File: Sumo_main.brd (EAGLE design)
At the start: 70 x 45 mm, 59 parts, among them IC1 TL331, T1 0603-PHOTO-TRANS, T2 0603-PHOTO-TRANS, U1 ATMEGA8U2AU, U2 SN65HVD3082, U3 LM339D, X2 RS485, Y1 16MHz

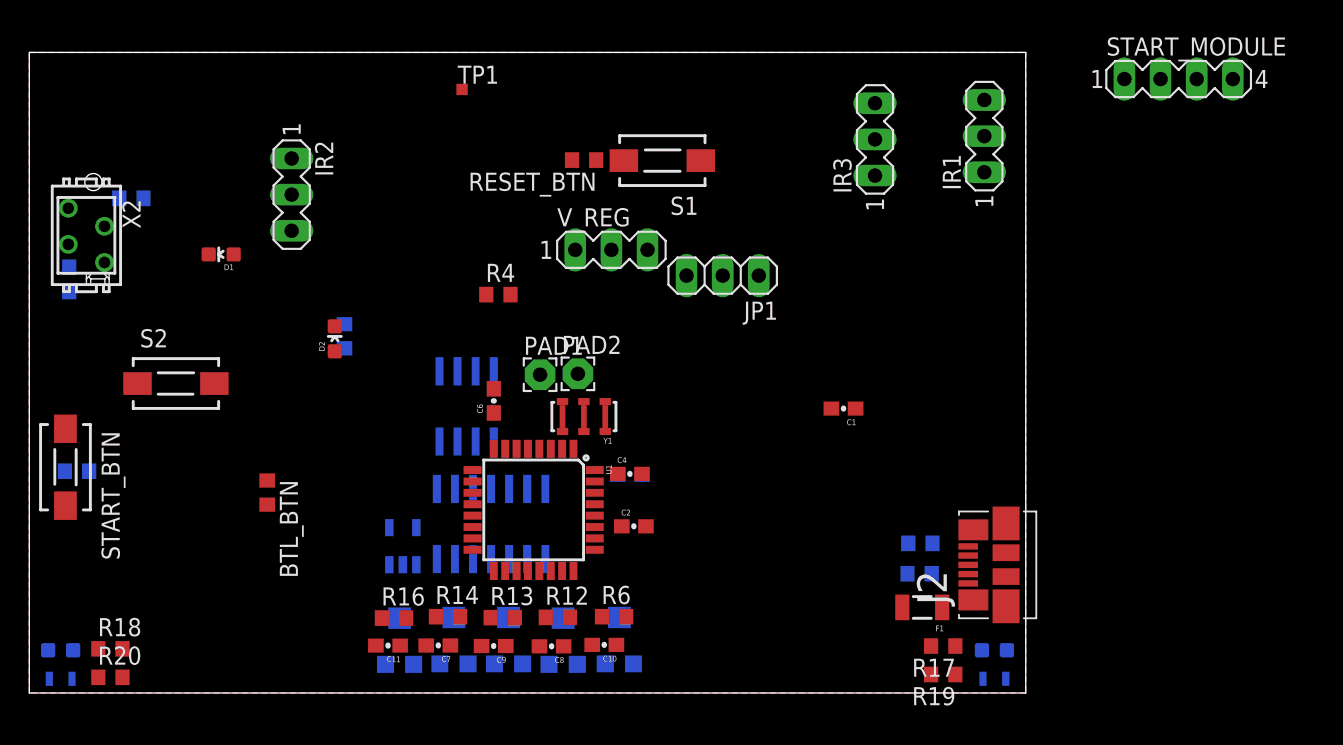
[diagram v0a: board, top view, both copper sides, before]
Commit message: Board redesign. TODO: Connect HWB
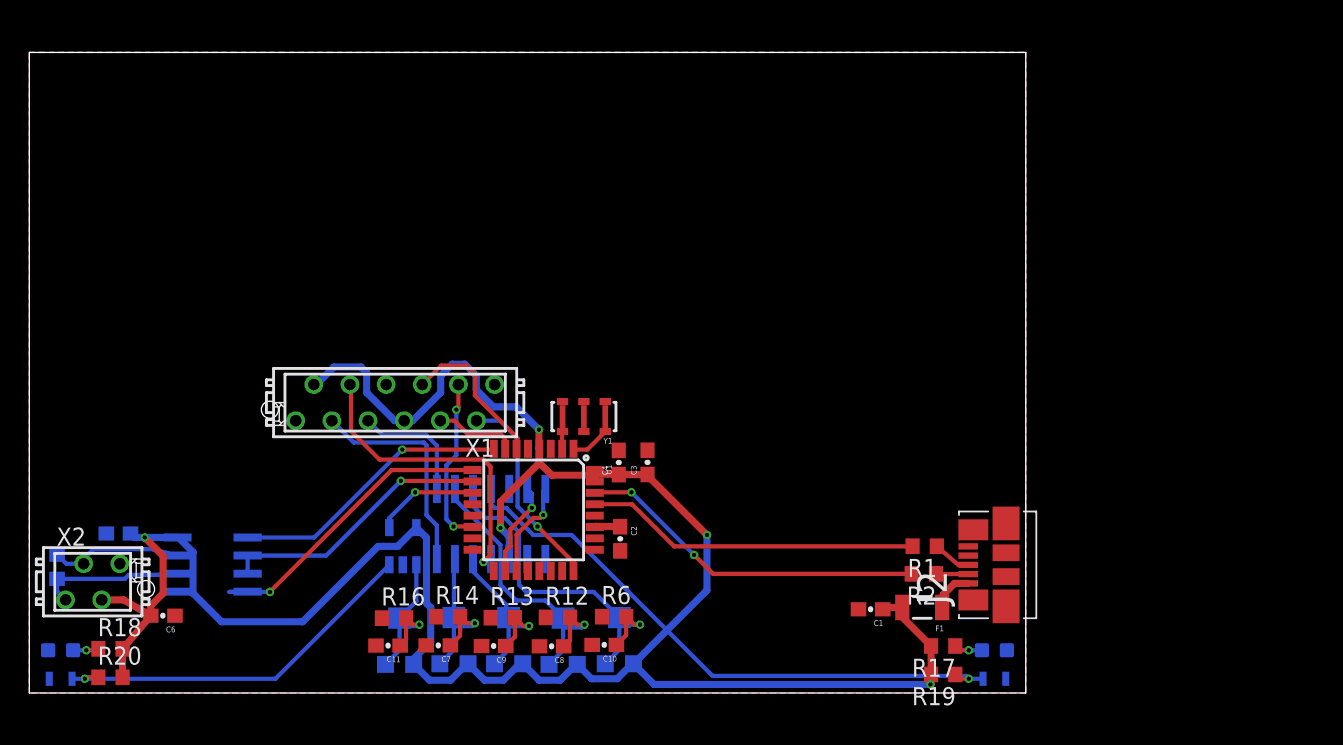
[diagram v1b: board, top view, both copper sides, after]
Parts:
- removed BTL_BTN, R7, RESET_BTN: 10K, resistor:R0603
- removed D1, D2: (no value), SparkFun-LED:LED-0603
- removed IR1, IR2, IR3, V_REG: (no value), con-lstb:MA03-1
- removed JP1: (no value), pinhead:1X03
- removed PAD1, PAD2: (no value), wirepad:2,15/1,0
- removed R4, R5: 1K, resistor:R0603
- removed S1, S2, START_BTN: DTSM-3, switch-tact:DTSM-3
- removed START_MODULE: (no value), con-lstb:MA04-1
- removed TP1: TPSQTP08SQ, testpad:TP08SQ
- added X1: MICROMATCH-12, con-amp-micromatch:MICROMATCH-12
- moved C6 27.7 mm to (9.38, 5.43), turned to 180 degrees
- moved R8 26.4 mm to (1.95, 8.87), turned to 270 degrees
- moved X2 24.3 mm to (4.45, 7.81), turned to 0 degrees
- moved U2 21.0 mm to (12.9, 9.02), turned to 0 degrees
- moved C5 18.2 mm to (6.26, 11.2), turned to 180 degrees
- moved C1 14.2 mm to (59.1, 5.88)
- moved C3 1.51 mm to (43.4, 16.2), flipped to the top, turned to 90 degrees
- moved C2 1.30 mm to (41.5, 10.8), turned to 270 degrees
- moved C4 1.12 mm to (41.4, 16.2), turned to 90 degrees
- moved R1 0.36 mm to (62.9, 10.3), flipped to the top, turned to 180 degrees
- moved R2 0.30 mm to (62.8, 8.37), flipped to the top, turned to 180 degrees
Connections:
- removed net LED1: R4.2, U1.5
- removed net LED2: R5.2, U1.26
- removed net N$10: D1.A, R4.1
- removed net N$12: F1.2, JP1.1
- removed net N$13: BTL_BTN.2, S2.2, U1.13
- removed net N$14: JP1.3, V_REG.3
- removed net N$17: U1.25
- removed net N$23: PAD1.1, V_REG.1
- removed net N$4: RESET_BTN.1, S1.2, U1.24
- removed net N$8: R7.1, START_BTN.2, U1.14
- removed net N$9: D2.A, R5.1
- new net HWB: U1.13, X1.12
- new net RESET: U1.24, X1.11
- new net START_BTN: U1.14, X1.10
- net GND: now also X1.1, X1.6; no longer D1.C, D2.C, IR1.2, IR2.2, IR3.2, PAD2.1, S1.1, S2.1, START_BTN.1, START_MODULE.2, V_REG.2
- net KILL: now also U1.6, X1.8; no longer START_MODULE.4, U1.23
- net START: now also U1.7, X1.9; no longer START_MODULE.3, U1.22
- net V01: now also X1.3; no longer IR1.3
- net V02: now also X1.4; no longer IR2.3
- net V03: now also X1.5; no longer IR3.3
- net VCC: now also F1.2, X1.2, X1.7; no longer BTL_BTN.1, IR1.1, IR2.1, IR3.1, JP1.2, R7.2, RESET_BTN.2, START_MODULE.1
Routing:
- net VCC: track 0.00 -> 161.3 mm, vias 0 -> 5
- net LN1: track 0.00 -> 41.8 mm, vias 0 -> 1
- net LN2: track 0.00 -> 26.6 mm, vias 0 -> 1
- net LN1REF: track 0.00 -> 25.5 mm, vias 0 -> 1
- net D-: track 0.00 -> 24.7 mm, vias 0 -> 2
- net D+: track 0.00 -> 23.9 mm
- net VREF3: track 0.00 -> 22.1 mm, vias 0 -> 1
- net TX: track 0.00 -> 21.9 mm, vias 0 -> 1
- net V02: track 0.00 -> 21.7 mm, vias 0 -> 1
- net RX: track 0.00 -> 19.9 mm, vias 0 -> 1
- net DE: track 0.00 -> 19.3 mm, vias 0 -> 1
- net V01: track 0.00 -> 15.7 mm
- net RESET: track 0.00 -> 14.4 mm, vias 0 -> 1
- net VREF2: track 0.00 -> 13.7 mm, vias 0 -> 1
- net VREF1: track 0.00 -> 12.9 mm, vias 0 -> 1
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
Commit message: Finish and fix errors of Main's schematic and board
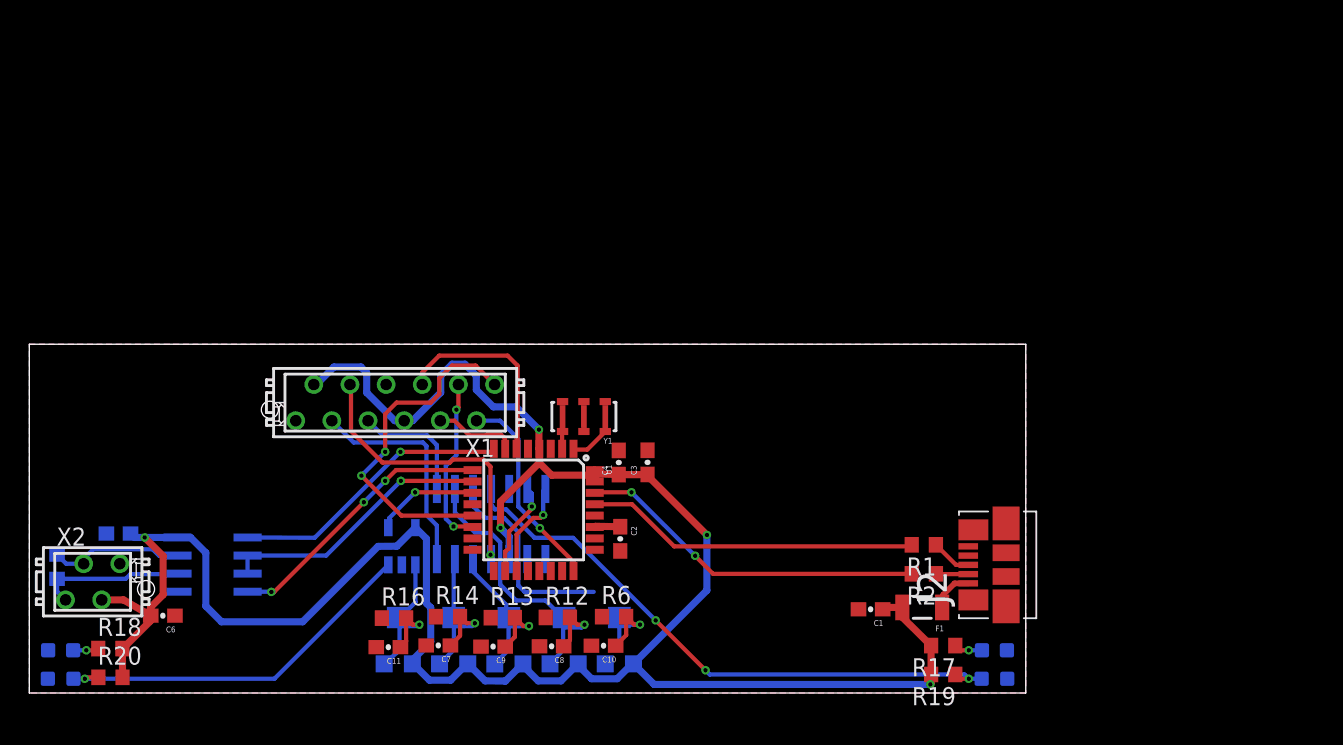
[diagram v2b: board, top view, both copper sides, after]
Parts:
- D3, D4: value (none) -> IR LED
- J2: value (none) -> MICRO_USB
- moved T2 0.80 mm to (2.20, 1.00)
- moved T1 0.80 mm to (67.8, 1.00)
- moved R1 0.12 mm to (62.8, 10.4)
- moved C11 0.11 mm to (25.2, 3.22)
- moved R15 0.10 mm to (25.9, 3.65)
- moved R9 0.08 mm to (37.6, 3.65)
- moved C10 0.08 mm to (40.3, 3.32)
- moved IC1 0.07 mm to (26.2, 10.3)
- moved C9 0.06 mm to (32.6, 3.26)
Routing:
- net HWB: track 0.00 -> 24.3 mm, vias 0 -> 2
- net LN1REF: track 25.5 -> 21.1 mm
- net KILL: track 11.0 -> 15.0 mm
- net TX: track 21.9 -> 19.4 mm, vias 1 -> 3
- net VCC: track 161.3 -> 162.6 mm
- net V02: track 21.7 -> 20.8 mm
- net VREF3: track 22.1 -> 22.8 mm
- net LN1: track 41.8 -> 41.7 mm, vias 1 -> 3
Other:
- board size 70 x 45 mm -> 70 x 24.5 mm

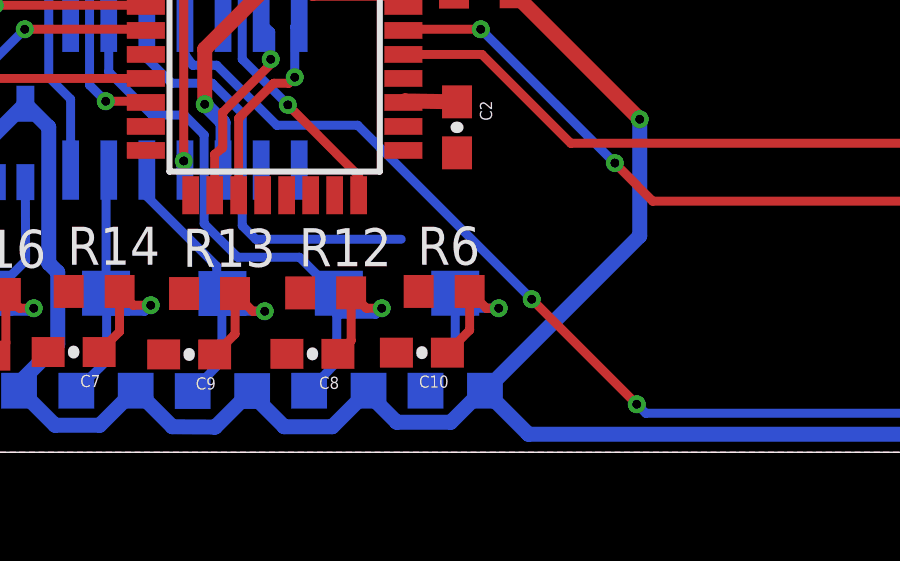
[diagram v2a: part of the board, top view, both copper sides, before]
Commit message: Wire one unwired signal
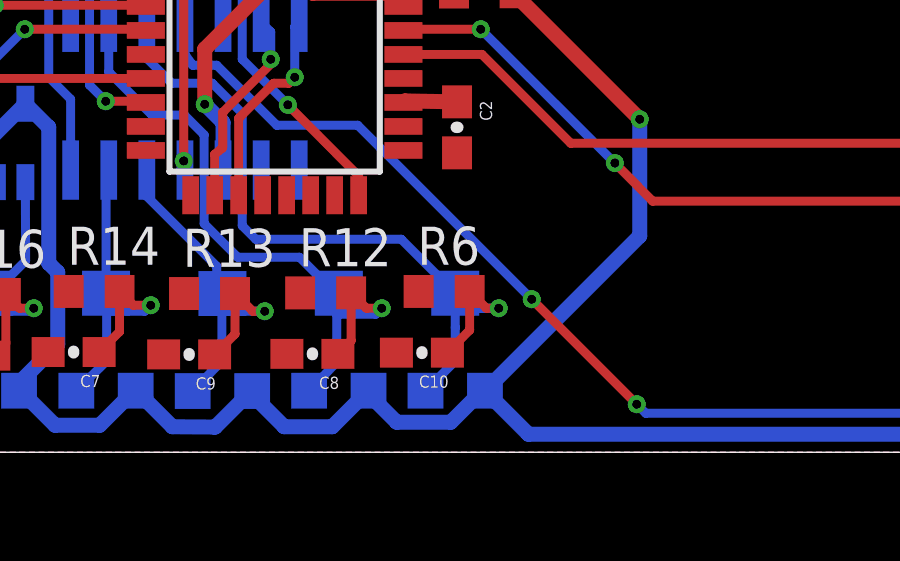
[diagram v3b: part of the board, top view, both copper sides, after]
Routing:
- net LN1REF: track 21.1 -> 26.7 mm
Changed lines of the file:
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@@
 <contactref element="R6" pad="2"/>
 <contactref element="C10" pad="1"/>
-<wire x1="41.45" y1="3.0404" x2="41.45" y2="4.8" width="0.3" layer="16"/>
+<wire x1="41.45" y1="4.16" x2="41.45" y2="4.8" width="0.3" layer="16"/>
 <wire x1="41.93" y1="5.36" x2="42.49" y2="4.8" width="0.3" layer="1"/>
 <wire x1="42.49" y1="4.8" x2="42.9" y2="4.8" width="0.3" layer="1"/>
@@
 <contactref element="R3" pad="3"/>
 <contactref element="R3" pad="2"/>
-<wire x1="41.93" y1="5.36" x2="41.45" y2="5.301" width="0" layer="19" extent="1-16"/>
-<wire x1="40.4594" y1="2.0498" x2="41.45" y2="3.0404" width="0" layer="19" extent="16-16"/>
-<wire x1="39.651" y1="7.1" x2="41.45" y2="5.301" width="0" layer="19" extent="16-16"/>
+<wire x1="39.651" y1="7.1" x2="41.45" y2="5.301" width="0.3" layer="16"/>
+<wire x1="41.45" y1="5.301" x2="41.951" y2="4.8" width="0.3" layer="16"/>
+<wire x1="41.951" y1="4.8" x2="42.9" y2="4.8" width="0.3" layer="16"/>
+<wire x1="40.4594" y1="2.0498" x2="41.45" y2="3.0404" width="0.3" layer="16"/>
+<wire x1="41.45" y1="3.0404" x2="41.45" y2="4.16" width="0.3" layer="16"/>
 </signal>
 <signal name="LN2REF">

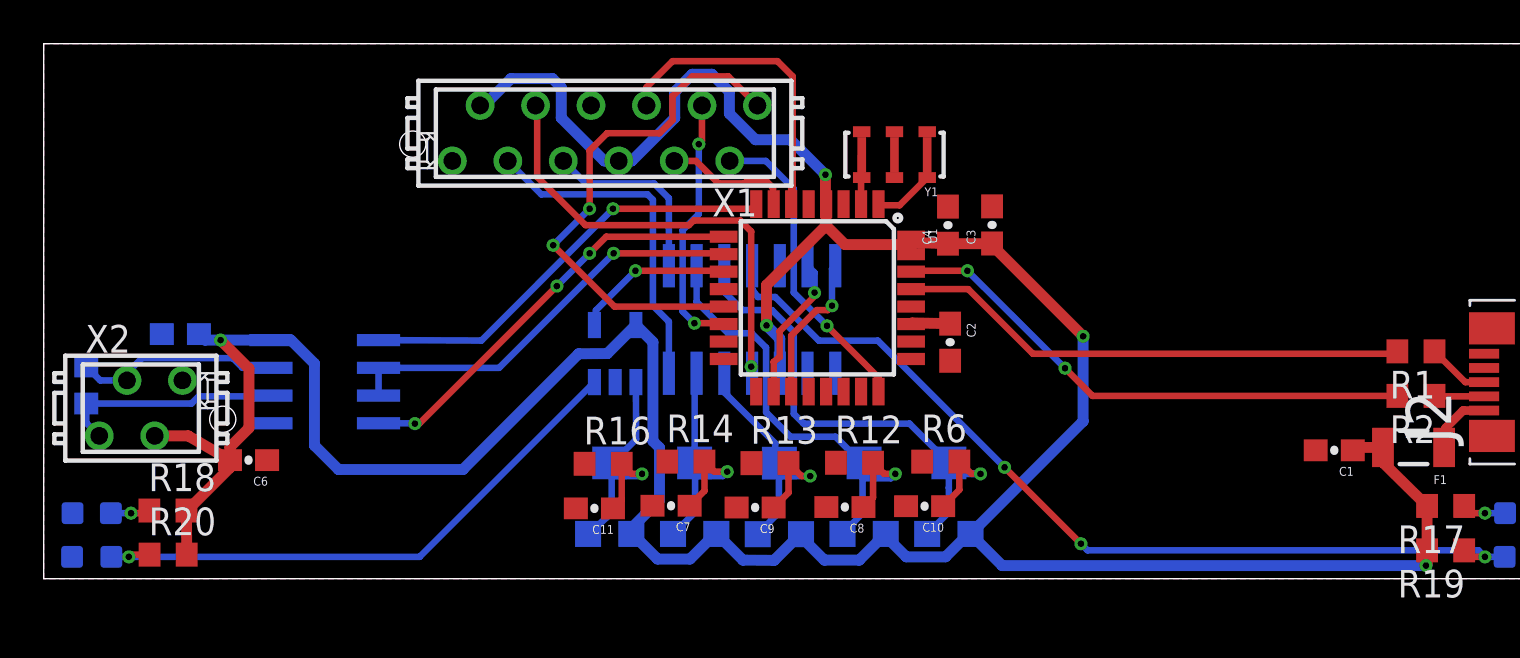
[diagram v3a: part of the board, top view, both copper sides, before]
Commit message: Add mounting holes to board and re-route some wires to get rid of some vias.
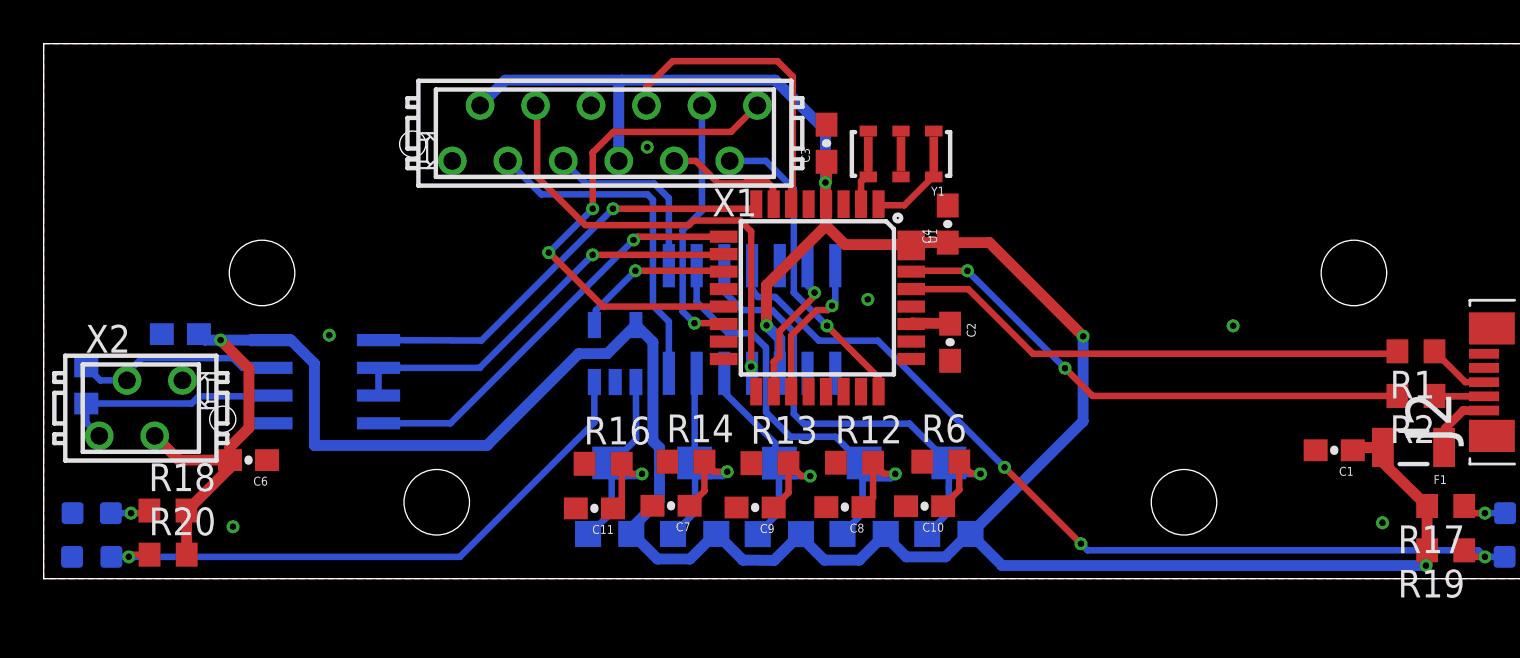
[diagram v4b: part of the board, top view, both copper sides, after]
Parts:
- moved C3 8.45 mm to (35.9, 19.9)
- moved Y1 0.30 mm to (39.3, 19.4)
- moved C4 0.05 mm to (41.4, 16.2)
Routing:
- net HWB: track 24.3 -> 23.1 mm
- net LN2: track 26.4 -> 27.5 mm
- net TX: track 19.4 -> 19.3 mm, vias 3 -> 1
- net START_BTN: vias 2 -> 1
